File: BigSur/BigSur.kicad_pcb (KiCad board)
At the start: 2 copper layers, 148 parts, among them J1 XT30PW-M, J10 XT30PW-M, J12 XT30PW-M, J14 XT30PW-M, J15 XT30PW-M, J16 XT30PW-M, J2 XT30PW-M, J3 XT30PW-M, J4 XT30PW-M, J5 XT30PW-M, J6 XT30PW-M, J7 XT30PW-M, J8 XT30PW-M, J9 XT30PW-M, K1 G5LE-1A-VDDC12, K2 G5LE-1A-VDDC12, K3 G5LE-1A-VDDC12, K4 G5LE-1A-VDDC12, Q1 TSM900N10, Q2 TSM900N10, Q3 MMBT3904-7-F, Q4 MMBT3904-7-F, Q5 MMBT3904-7-F, Q6 MMBT3904-7-F, U1 DRV103H, U10 MCP6L02T-E_MS, U11 74LVC1G08W5-7, U12 ACS70331EESATR-2P5U3, U2 DRV103H, U3 DRV8806, U4 SMD46, U5 ACS70331EESATR-2P5U3, U6 ACS70331EESATR-2P5U3, U7 ACS70331EESATR-2P5U3, U8 ACS70331EESATR-2P5U3, U9 ACS70331EESATR-2P5U3

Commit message: Initial layout pass. This will be changed many times I'm sure.
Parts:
- C1: moved to F.Cu
- C36, C37, C38, C39, D1, D14, D15, D18, D19, D5, Q1, Q2, Q3, Q4, Q5, Q6, R12, R13, R15, R16, R17, R18, R23, R24, R25, R26, R29, R3, R30, R31, R32, R6, U11, U6, U8: moved to B.Cu
- moved D14 180.3 mm to (51.5, 115.0), turned to 90 degrees
- moved Q3 174.5 mm to (46.5, 115.0), turned to 270 degrees
- moved C18 171.9 mm to (36.5, 83.0)
- moved D15 166.6 mm to (70.0, 115.0), turned to 90 degrees
- moved D18 166.1 mm to (88.2, 115.0), turned to 90 degrees
- moved TP1 164.8 mm to (45.0, 48.5)
- moved D19 164.7 mm to (108.0, 115.0), turned to 90 degrees
- moved Q5 164.0 mm to (65.0, 115.0), turned to 270 degrees
- moved TP2 164.0 mm to (45.0, 52.5)
- moved TP3 163.5 mm to (45.0, 56.5)
- moved D20 163.4 mm to (69.0, 109.0)
- moved R20 161.1 mm to (93.2, 75.5)
- moved R14 160.1 mm to (93.2, 73.5), turned to 180 degrees
- moved D17 160.0 mm to (87.2, 109.0)
- moved Q6 160.0 mm to (103.0, 115.0), turned to 270 degrees
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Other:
- board outline added: 123.5 x 131.5 mm

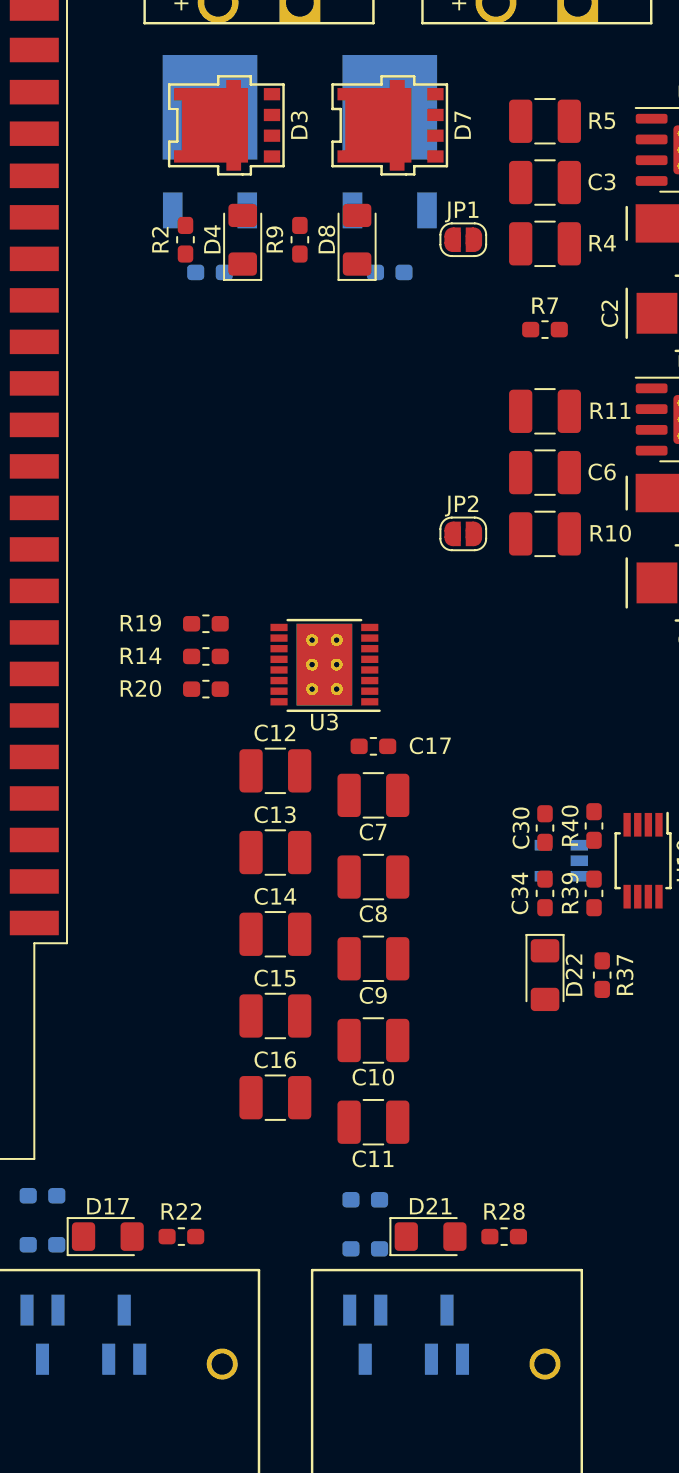
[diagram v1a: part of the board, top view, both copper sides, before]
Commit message: Moved configuration passives for DRV103s.
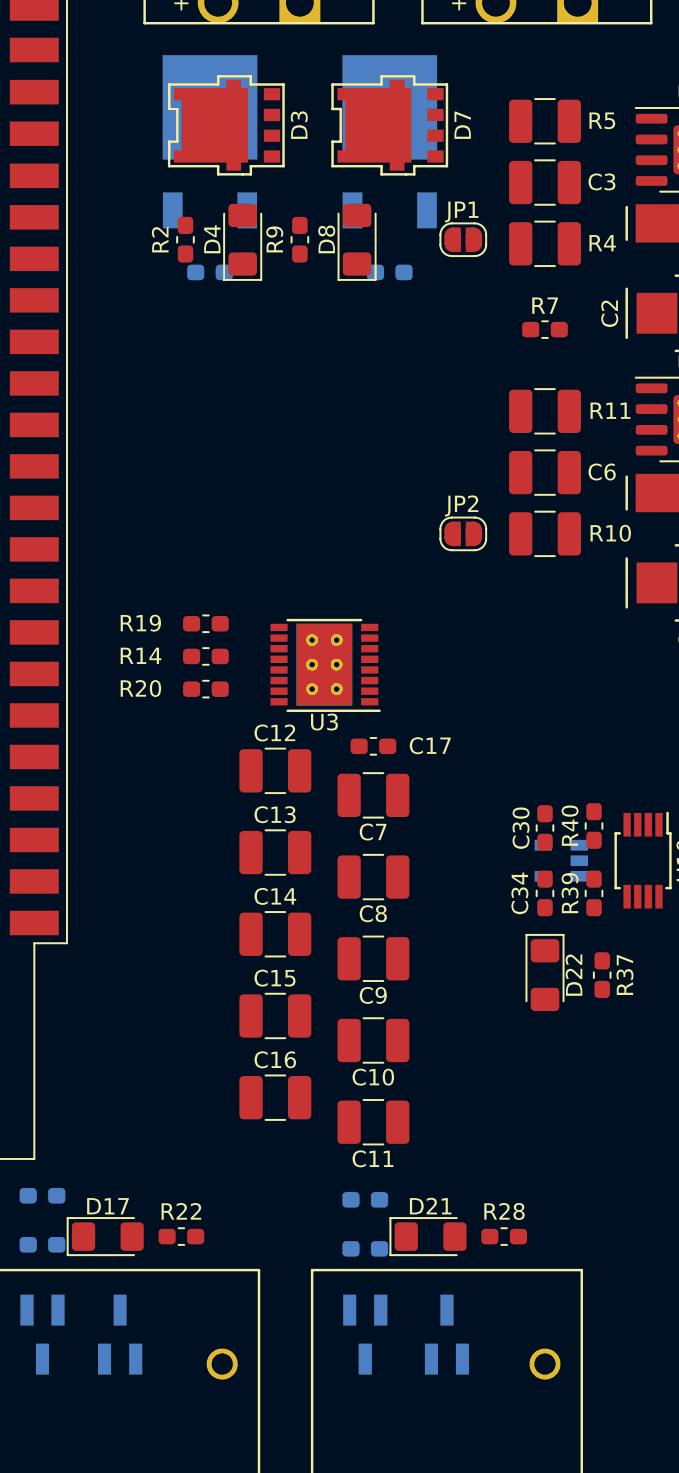
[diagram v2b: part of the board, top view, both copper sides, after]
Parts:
- moved D18 18.2 mm to (70.0, 115.0)
- moved D15 18.0 mm to (88.0, 115.0)
- turned C3 to 180 degrees
- turned C6 to 180 degrees
- turned R10 to 180 degrees
- turned R11 to 180 degrees
- turned R4 to 180 degrees
- turned R5 to 180 degrees
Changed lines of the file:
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@@
   )
   (module Capacitor_SMD:C_1210_3225Metric_Pad1.42x2.65mm_HandSolder (layer F.Cu)
-    (at 114 44.5)
+    (at 114 44.5 180)
     (descr "Capacitor SMD 1210 (3225 Metric), square (rectangular) end terminal, IPC_7351 nominal with elongated pad for handsoldering. (Body size source: http://www.tortai-tech.com/upload/download/2011102023233369053.pdf), generated with kicad-footprint-generator")
     (tags "capacitor handsolder")
     (attr smd)
-    (fp_text reference C3 (at 3.5 0) (layer F.SilkS)
+    (fp_text reference C3 (at -3.5 0) (layer F.SilkS)
       (effects (font (size 1 1) (thickness 0.15)))
     )
@@
       (effects (font (size 0.8 0.8) (thickness 0.12)))
     )
-    (pad 1 smd roundrect (at -1.4875 0) (size 1.425 2.65) (layers F.Cu F.Paste F.Mask) (roundrect_rratio 0.175439)
+    (pad 1 smd roundrect (at -1.4875 0 180) (size 1.425 2.65) (layers F.Cu F.Paste F.Mask) (roundrect_rratio 0.175439)
       (net 3 "Net-(C3-Pad1)"))
-    (pad 2 smd roundrect (at 1.4875 0) (size 1.425 2.65) (layers F.Cu F.Paste F.Mask) (roundrect_rratio 0.175439)
+    (pad 2 smd roundrect (at 1.4875 0 180) (size 1.425 2.65) (layers F.Cu F.Paste F.Mask) (roundrect_rratio 0.175439)
       (net 1 GND))
     (model ${KISYS3DMOD}/Capacitor_SMD.3dshapes/C_1210_3225Metric.wrl
@@
   )
   (module Capacitor_SMD:C_1210_3225Metric_Pad1.42x2.65mm_HandSolder (layer F.Cu)
-    (at 114 62.25)
+    (at 114 62.25 180)
     (descr "Capacitor SMD 1210 (3225 Metric), square (rectangular) end terminal, IPC_7351 nominal with elongated pad for handsoldering. (Body size source: http://www.tortai-tech.com/upload/download/2011102023233369053.pdf), generated with kicad-footprint-generator")
     (tags "capacitor handsolder")
     (attr smd)
-    (fp_text reference C6 (at 3.5 0) (layer F.SilkS)
+    (fp_text reference C6 (at -3.5 0) (layer F.SilkS)
       (effects (font (size 1 1) (thickness 0.15)))
     )
@@
     (fp_line (start -1.6 -1.25) (end 1.6 -1.25) (layer F.Fab) (width 0.1))
     (fp_line (start -1.6 1.25) (end -1.6 -1.25) (layer F.Fab) (width 0.1))
-    (pad 2 smd roundrect (at 1.4875 0) (size 1.425 2.65) (layers F.Cu F.Paste F.Mask) (roundrect_rratio 0.175439)
+    (pad 2 smd roundrect (at 1.4875 0 180) (size 1.425 2.65) (layers F.Cu F.Paste F.Mask) (roundrect_rratio 0.175439)
       (net 1 GND))
-    (pad 1 smd roundrect (at -1.4875 0) (size 1.425 2.65) (layers F.Cu F.Paste F.Mask) (roundrect_rratio 0.175439)
+    (pad 1 smd roundrect (at -1.4875 0 180) (size 1.425 2.65) (layers F.Cu F.Paste F.Mask) (roundrect_rratio 0.175439)
       (net 4 "Net-(C6-Pad1)"))
     (model ${KISYS3DMOD}/Capacitor_SMD.3dshapes/C_1210_3225Metric.wrl
@@
   )
   (module Package_TO_SOT_SMD:SOT-23_Handsoldering (layer B.Cu)
-    (at 70 115 90)
+    (at 88 115 90)
     (descr "SOT-23, Handsoldering")
     (tags SOT-23)
@@
   )
   (module Package_TO_SOT_SMD:SOT-23_Handsoldering (layer B.Cu)
-    (at 88.25 115 90)
+    (at 70 115 90)
     (descr "SOT-23, Handsoldering")
     (tags SOT-23)
@@
   )
   (module Resistor_SMD:R_1210_3225Metric_Pad1.42x2.65mm_HandSolder (layer F.Cu)
-    (at 114 48.25)
+    (at 114 48.25 180)
     (descr "Resistor SMD 1210 (3225 Metric), square (rectangular) end terminal, IPC_7351 nominal with elongated pad for handsoldering. (Body size source: http://www.tortai-tech.com/upload/download/2011102023233369053.pdf), generated with kicad-footprint-generator")
     (tags "resistor handsolder")
     (attr smd)
-    (fp_text reference R4 (at 3.5 0) (layer F.SilkS)
+    (fp_text reference R4 (at -3.5 0) (layer F.SilkS)
       (effects (font (size 1 1) (thickness 0.15)))
     )
@@
     (fp_line (start -1.6 -1.25) (end 1.6 -1.25) (layer F.Fab) (width 0.1))
     (fp_line (start -1.6 1.25) (end -1.6 -1.25) (layer F.Fab) (width 0.1))
-    (pad 2 smd roundrect (at 1.4875 0) (size 1.425 2.65) (layers F.Cu F.Paste F.Mask) (roundrect_rratio 0.175439)
+    (pad 2 smd roundrect (at 1.4875 0 180) (size 1.425 2.65) (layers F.Cu F.Paste F.Mask) (roundrect_rratio 0.175439)
       (net 1 GND))
-    (pad 1 smd roundrect (at -1.4875 0) (size 1.425 2.65) (layers F.Cu F.Paste F.Mask) (roundrect_rratio 0.175439)
+    (pad 1 smd roundrect (at -1.4875 0 180) (size 1.425 2.65) (layers F.Cu F.Paste F.Mask) (roundrect_rratio 0.175439)
       (net 62 "Net-(JP1-Pad2)"))
     (model ${KISYS3DMOD}/Resistor_SMD.3dshapes/R_1210_3225Metric.wrl
@@
   )
   (module Resistor_SMD:R_1210_3225Metric_Pad1.42x2.65mm_HandSolder (layer F.Cu)
-    (at 114 40.75)
+    (at 114 40.75 180)
     (descr "Resistor SMD 1210 (3225 Metric), square (rectangular) end terminal, IPC_7351 nominal with elongated pad for handsoldering. (Body size source: http://www.tortai-tech.com/upload/download/2011102023233369053.pdf), generated with kicad-footprint-generator")
     (tags "resistor handsolder")
     (attr smd)
-    (fp_text reference R5 (at 3.5 0) (layer F.SilkS)
+    (fp_text reference R5 (at -3.5 0) (layer F.SilkS)
       (effects (font (size 1 1) (thickness 0.15)))
     )
@@
       (effects (font (size 0.8 0.8) (thickness 0.12)))
     )
-    (pad 1 smd roundrect (at -1.4875 0) (size 1.425 2.65) (layers F.Cu F.Paste F.Mask) (roundrect_rratio 0.175439)
+    (pad 1 smd roundrect (at -1.4875 0 180) (size 1.425 2.65) (layers F.Cu F.Paste F.Mask) (roundrect_rratio 0.175439)
       (net 71 "Net-(R5-Pad1)"))
-    (pad 2 smd roundrect (at 1.4875 0) (size 1.425 2.65) (layers F.Cu F.Paste F.Mask) (roundrect_rratio 0.175439)
+    (pad 2 smd roundrect (at 1.4875 0 180) (size 1.425 2.65) (layers F.Cu F.Paste F.Mask) (roundrect_rratio 0.175439)
       (net 1 GND))
     (model ${KISYS3DMOD}/Resistor_SMD.3dshapes/R_1210_3225Metric.wrl
@@
   )
   (module Resistor_SMD:R_1210_3225Metric_Pad1.42x2.65mm_HandSolder (layer F.Cu)
-    (at 114 66)
+    (at 114 66 180)
     (descr "Resistor SMD 1210 (3225 Metric), square (rectangular) end terminal, IPC_7351 nominal with elongated pad for handsoldering. (Body size source: http://www.tortai-tech.com/upload/download/2011102023233369053.pdf), generated with kicad-footprint-generator")
     (tags "resistor handsolder")
     (attr smd)
-    (fp_text reference R10 (at 4 0) (layer F.SilkS)
+    (fp_text reference R10 (at -4 0) (layer F.SilkS)
       (effects (font (size 1 1) (thickness 0.15)))
     )
@@
     (fp_line (start -1.6 -1.25) (end 1.6 -1.25) (layer F.Fab) (width 0.1))
     (fp_line (start -1.6 1.25) (end -1.6 -1.25) (layer F.Fab) (width 0.1))
-    (pad 2 smd roundrect (at 1.4875 0) (size 1.425 2.65) (layers F.Cu F.Paste F.Mask) (roundrect_rratio 0.175439)
+    (pad 2 smd roundrect (at 1.4875 0 180) (size 1.425 2.65) (layers F.Cu F.Paste F.Mask) (roundrect_rratio 0.175439)
       (net 1 GND))
-    (pad 1 smd roundrect (at -1.4875 0) (size 1.425 2.65) (layers F.Cu F.Paste F.Mask) (roundrect_rratio 0.175439)
+    (pad 1 smd roundrect (at -1.4875 0 180) (size 1.425 2.65) (layers F.Cu F.Paste F.Mask) (roundrect_rratio 0.175439)
       (net 63 "Net-(JP2-Pad2)"))
     (model ${KISYS3DMOD}/Resistor_SMD.3dshapes/R_1210_3225Metric.wrl
@@
   )
   (module Resistor_SMD:R_1210_3225Metric_Pad1.42x2.65mm_HandSolder (layer F.Cu)
-    (at 114 58.5)
+    (at 114 58.5 180)
     (descr "Resistor SMD 1210 (3225 Metric), square (rectangular) end terminal, IPC_7351 nominal with elongated pad for handsoldering. (Body size source: http://www.tortai-tech.com/upload/download/2011102023233369053.pdf), generated with kicad-footprint-generator")
     (tags "resistor handsolder")
     (attr smd)
-    (fp_text reference R11 (at 4 0) (layer F.SilkS)
+    (fp_text reference R11 (at -4 0) (layer F.SilkS)
       (effects (font (size 1 1) (thickness 0.15)))
     )
@@
       (effects (font (size 0.8 0.8) (thickness 0.12)))
     )
-    (pad 1 smd roundrect (at -1.4875 0) (size 1.425 2.65) (layers F.Cu F.Paste F.Mask) (roundrect_rratio 0.175439)
+    (pad 1 smd roundrect (at -1.4875 0 180) (size 1.425 2.65) (layers F.Cu F.Paste F.Mask) (roundrect_rratio 0.175439)
       (net 74 "Net-(R11-Pad1)"))
-    (pad 2 smd roundrect (at 1.4875 0) (size 1.425 2.65) (layers F.Cu F.Paste F.Mask) (roundrect_rratio 0.175439)
+    (pad 2 smd roundrect (at 1.4875 0 180) (size 1.425 2.65) (layers F.Cu F.Paste F.Mask) (roundrect_rratio 0.175439)
       (net 1 GND))
     (model ${KISYS3DMOD}/Resistor_SMD.3dshapes/R_1210_3225Metric.wrl

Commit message: Moved some things.
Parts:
- moved C11 46.1 mm to (91.5, 57.5), turned to 0 degrees
- moved C16 41.5 mm to (97.5, 59.0), turned to 180 degrees
- moved C10 36.5 mm to (91.5, 62.5), turned to 0 degrees
- moved C15 31.5 mm to (97.5, 64.0), turned to 180 degrees
- moved C9 27.3 mm to (91.5, 67.5), turned to 0 degrees
- moved C14 21.5 mm to (97.5, 69.0), turned to 180 degrees
- moved C8 18.8 mm to (91.5, 72.5), turned to 0 degrees
- moved R19 18.6 mm to (101.8, 88.0), turned to 180 degrees
- moved R14 15.1 mm to (101.8, 86.0), turned to 0 degrees
- moved U3 13.0 mm to (94.5, 85.5)
- moved C7 12.8 mm to (91.5, 77.5), turned to 0 degrees
- moved C17 12.1 mm to (91.5, 80.5), turned to 0 degrees
- moved R20 12.0 mm to (101.8, 84.0), turned to 180 degrees
- moved C13 11.5 mm to (97.5, 74.0), turned to 180 degrees
- moved C12 1.50 mm to (97.5, 79.0), turned to 180 degrees
